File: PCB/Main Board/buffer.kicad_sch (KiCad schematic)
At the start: 0 parts

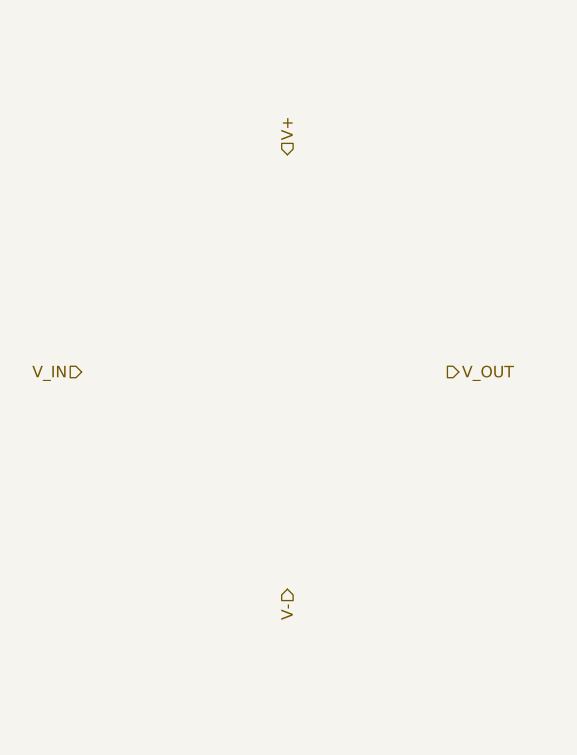
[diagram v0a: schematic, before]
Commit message: created buffer subcircuit
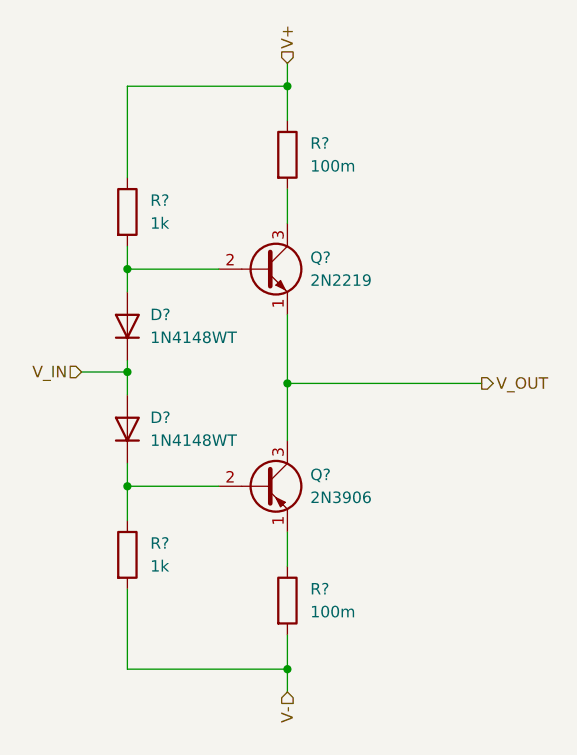
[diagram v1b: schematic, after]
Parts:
- added D? (x2): 1N4148WT, Diode_SMD:D_SOD-523, symbol Diode:1N4148WT
- added Q?: 2N3906, Package_TO_SOT_THT:TO-92_Inline, symbol Transistor_BJT:2N3906
- added Q?: 2N2219, Package_TO_SOT_THT:TO-39-3, symbol Transistor_BJT:2N2219
- added R? (x2): 100m, symbol Device:R
- added R? (x2): 1k, symbol Device:R
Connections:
- net  V- : now also R?.2, R?.2
- net V+: now also R?.1, R?.1
- net V_IN: now also D?.1 (K), D?.2 (A)
- net V_OUT: now also Q?.1 (E), Q?.3 (C)
- new net: D?.1 (K), Q?.2 (B), R?.1
- new net: Q?.1 (E), R?.1
- new net: Q?.3 (C), R?.2
- new net: D?.2 (A), Q?.2 (B), R?.2
